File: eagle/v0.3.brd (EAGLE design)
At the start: 30.1 x 52.1 mm, 15 parts

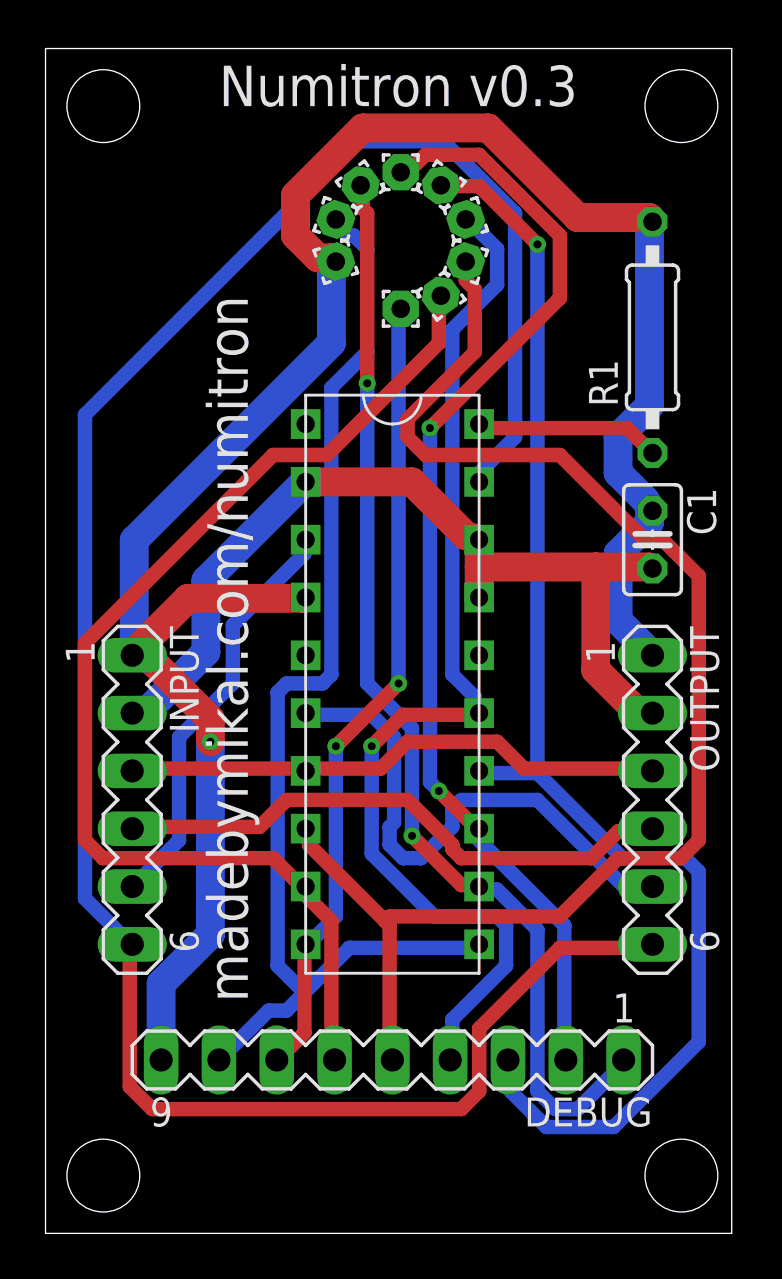
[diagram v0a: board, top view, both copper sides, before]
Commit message: Add another filter cap as recommended by Hugh Blemings.
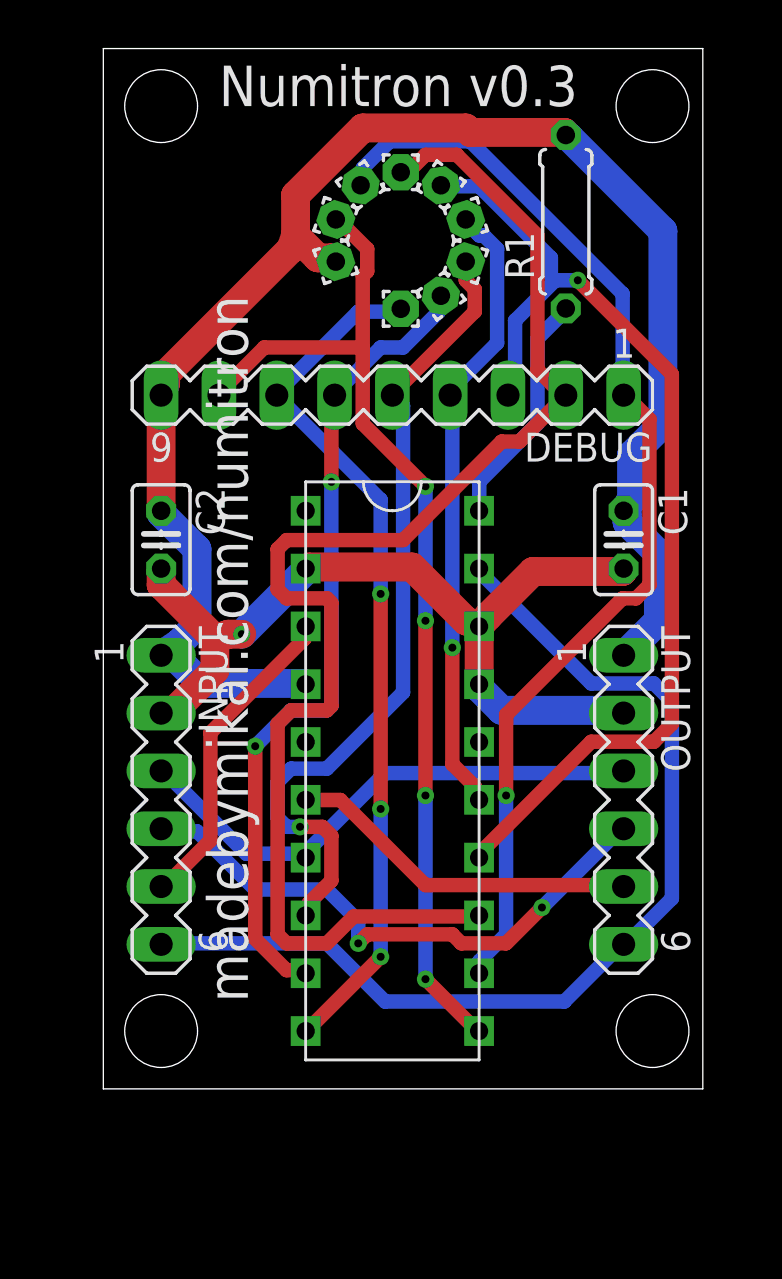
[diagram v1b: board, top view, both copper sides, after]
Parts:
- added C2: 47uF, rcl:C025-025X050
- R1: device rcl:0207/10 -> rcl:0207/7
- moved DEBUG 29.2 mm to (49.5, 43.2)
- moved R1 6.35 mm to (57.1, 50.8)
- moved U$1 3.81 mm to (49.5, 26.7)
- moved C1 1.27 mm to (59.7, 36.8)
- moved OUTPUT 1.27 mm to (59.7, 25.4)
- moved INPUT 1.27 mm to (39.4, 25.4)
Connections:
- net GND: now also C2.2
- net VCC: now also C2.1
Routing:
- net G: track 96.1 -> 45.0 mm
- net N$5: track 63.1 -> 36.1 mm, vias 0 -> 1
- net VCC: track 94.4 -> 73.0 mm, vias 1 -> 0
- net N$4: track 48.0 -> 27.6 mm
- net N$6: track 50.5 -> 36.0 mm, vias 0 -> 2
- net N$3: track 59.4 -> 46.3 mm
- net N$2: track 49.9 -> 61.2 mm, vias 2 -> 0
- net N$10: track 24.0 -> 15.6 mm
- net N$8: track 51.2 -> 45.9 mm, vias 0 -> 4
- net N$9: track 18.4 -> 14.3 mm
- net N$7: track 35.3 -> 38.3 mm, vias 2 -> 3
- net N$19: track 8.24 -> 10.5 mm
- net GND: track 40.3 -> 39.6 mm, vias 0 -> 1
- net RCK: track 25.1 -> 25.5 mm, vias 0 -> 2
- net N$1: track 49.0 -> 49.3 mm, vias 2 -> 1
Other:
- board size 30.1 x 52.1 mm -> 26.3 x 45.7 mm
